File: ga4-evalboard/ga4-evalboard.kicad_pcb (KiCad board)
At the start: 2 copper layers, 21.6 x 21.5 mm, 8 parts, among them J1 power, J2 analog, J3 Conn_01x04_Male, J4 Conn_01x04_Male, U1 GA4, U4 SST25WF080B

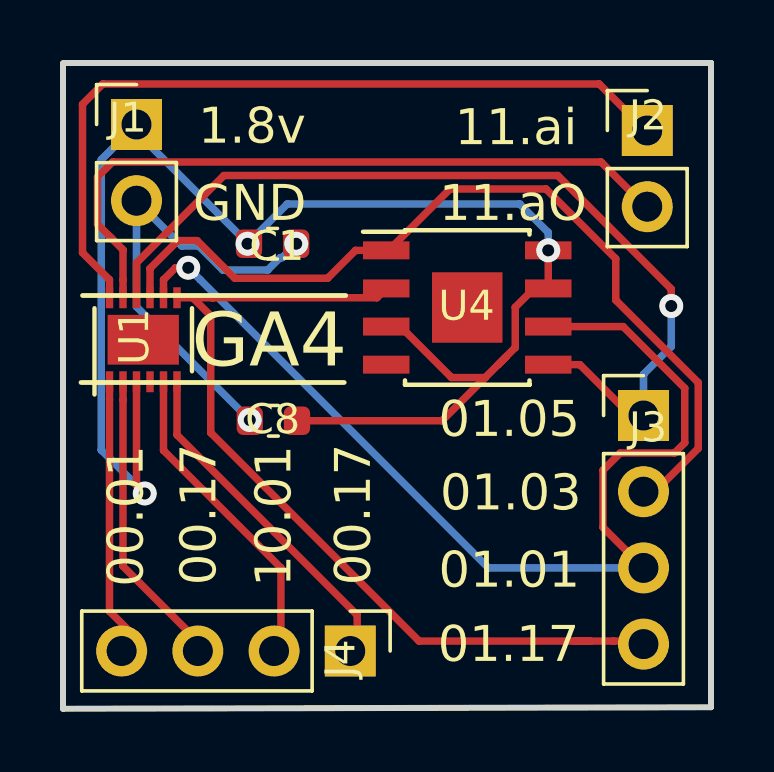
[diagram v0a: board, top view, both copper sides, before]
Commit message: ga4 evalboard layout changes
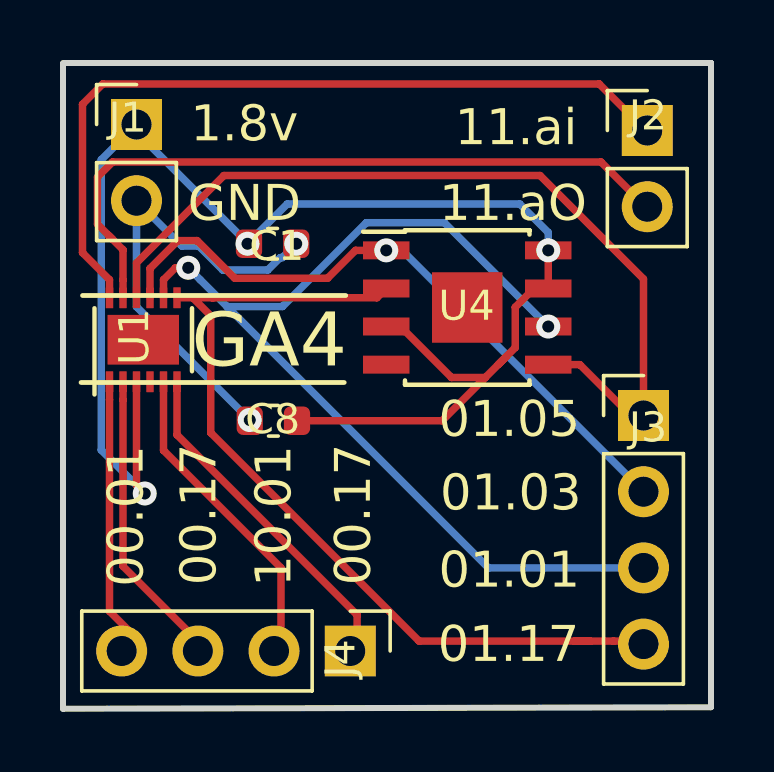
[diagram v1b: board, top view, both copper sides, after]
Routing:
- net 01.03: track 29.2 -> 22.0 mm, vias 0 -> 1
- net 01.05: track 30.2 -> 29.1 mm, vias 1 -> 0
- net 01.01: track 35.0 -> 34.2 mm, vias 1 -> 2
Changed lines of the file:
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@@
-(kicad_pcb (version 20171130) (host pcbnew 5.0.1-33cea8e~68~ubuntu14.04.1)
+(kicad_pcb (version 20171130) (host pcbnew 5.0.2-bee76a0~70~ubuntu14.04.1)
   (general
     (thickness 1.6)
     (drawings 19)
-    (tracks 122)
+    (tracks 111)
     (zones 0)
     (modules 8)
@@
     (effects (font (size 1.2 1.2) (thickness 0.25)))
   )
-  (gr_text GND (at 139.625 96.125) (layer F.SilkS)
-    (effects (font (size 1.2 1.2) (thickness 0.25)))
-  )
-  (gr_text 1.8v (at 139.7 93.55) (layer F.SilkS)
+  (gr_text GND (at 139.446 96.125) (layer F.SilkS)
+    (effects (font (size 1.2 1.2) (thickness 0.25)))
+  )
+  (gr_text 1.8v (at 139.446 93.472) (layer F.SilkS)
     (effects (font (size 1.2 1.2) (thickness 0.25)))
   )
@@
   )
   (via (at 139.625 103.35) (size 0.8) (drill 0.4) (layers F.Cu B.Cu) (net 1))
-  (via (at 139.55 97.475) (size 0.8) (drill 0.4) (layers F.Cu B.Cu) (net 2))
   (via (at 141.175 97.475) (size 0.8) (drill 0.4) (layers F.Cu B.Cu) (net 1))
   (segment (start 135.85 99.575) (end 139.625 103.35) (width 0.25) (layer B.Cu) (net 1))
@@
   (segment (start 140.225 98.35) (end 138.722682 98.35) (width 0.25) (layer B.Cu) (net 1))
   (segment (start 137.360159 97.550159) (end 135.85 96.04) (width 0.25) (layer B.Cu) (net 1))
-  (segment (start 135.4 98.675) (end 135.4 99.275) (width 0.25) (layer F.Cu) (net 4))
-  (segment (start 135.4 98.675) (end 135.4 97.675) (width 0.25) (layer F.Cu) (net 4))
-  (segment (start 135.05 97.325) (end 134.925 97.2) (width 0.25) (layer F.Cu) (net 4))
-  (segment (start 135.4 97.675) (end 135.05 97.325) (width 0.25) (layer F.Cu) (net 4))
-  (via (at 153.67516 99.54984) (size 0.8) (drill 0.4) (layers F.Cu B.Cu) (net 5))
+  (via (at 139.55 97.475) (size 0.8) (drill 0.4) (layers F.Cu B.Cu) (net 2))
   (segment (start 149.575 97.695) (end 149.575 97.695) (width 0.25) (layer F.Cu) (net 2))
   (via (at 136.125 105.8) (size 0.8) (drill 0.4) (layers F.Cu B.Cu) (net 2))
@@
   (segment (start 151.275 92.15) (end 134.725 92.15) (width 0.25) (layer F.Cu) (net 3))
   (segment (start 152.775 93.65) (end 151.275 92.15) (width 0.25) (layer F.Cu) (net 3))
+  (segment (start 135.4 98.675) (end 135.4 99.275) (width 0.25) (layer F.Cu) (net 4))
+  (segment (start 135.4 98.675) (end 135.4 97.675) (width 0.25) (layer F.Cu) (net 4))
+  (segment (start 135.05 97.325) (end 134.925 97.2) (width 0.25) (layer F.Cu) (net 4))
+  (segment (start 135.4 97.675) (end 135.05 97.325) (width 0.25) (layer F.Cu) (net 4))
   (segment (start 134.55 96.825) (end 135.05 97.325) (width 0.25) (layer F.Cu) (net 4))
   (segment (start 151.334978 94.749978) (end 135.050022 94.749978) (width 0.25) (layer F.Cu) (net 4))
@@
   (segment (start 150.63 101.505) (end 152.325 103.2) (width 0.25) (layer F.Cu) (net 5))
   (segment (start 149.575 101.505) (end 150.63 101.505) (width 0.25) (layer F.Cu) (net 5))
-  (segment (start 153.67516 100.89984) (end 153.67516 99.54984) (width 0.25) (layer B.Cu) (net 5))
-  (segment (start 152.75 101.825) (end 153.67516 100.89984) (width 0.25) (layer B.Cu) (net 5))
-  (segment (start 152.75 103.2) (end 152.75 101.825) (width 0.25) (layer B.Cu) (net 5))
-  (segment (start 149.890994 95.199989) (end 153.67516 98.984155) (width 0.25) (layer F.Cu) (net 5))
+  (segment (start 152.75 98.648) (end 152.75 103.2) (width 0.25) (layer F.Cu) (net 5))
+  (segment (start 149.301989 95.199989) (end 152.75 98.648) (width 0.25) (layer F.Cu) (net 5))
+  (segment (start 138.7636 95.199989) (end 149.301989 95.199989) (width 0.25) (layer F.Cu) (net 5))
+  (segment (start 135.85 98.113589) (end 138.7636 95.199989) (width 0.25) (layer F.Cu) (net 5))
   (segment (start 135.85 99.275) (end 135.85 98.113589) (width 0.25) (layer F.Cu) (net 5))
-  (segment (start 138.7636 95.199989) (end 149.890994 95.199989) (width 0.25) (layer F.Cu) (net 5))
-  (segment (start 135.85 98.113589) (end 138.7636 95.199989) (width 0.25) (layer F.Cu) (net 5))
-  (segment (start 153.67516 98.984155) (end 153.67516 99.54984) (width 0.25) (layer F.Cu) (net 5))
   (segment (start 136.3 98.3) (end 136.3 99.275) (width 0.25) (layer F.Cu) (net 6))
   (segment (start 137.870057 97.370057) (end 137.229943 97.370057) (width 0.25) (layer F.Cu) (net 6))
@@
   (segment (start 143.15 97.695) (end 142.22 98.625) (width 0.25) (layer F.Cu) (net 6))
   (segment (start 144.175 97.695) (end 143.15 97.695) (width 0.25) (layer F.Cu) (net 6))
-  (segment (start 153.231413 105.64) (end 152.95 105.64) (width 0.25) (layer F.Cu) (net 6))
-  (segment (start 154.57499 104.296423) (end 153.231413 105.64) (width 0.25) (layer F.Cu) (net 6))
-  (segment (start 154.57499 102.103577) (end 154.57499 104.296423) (width 0.25) (layer F.Cu) (net 6))
-  (segment (start 151.825 99.353587) (end 154.57499 102.103577) (width 0.25) (layer F.Cu) (net 6))
-  (segment (start 151.825 97.975) (end 151.825 99.353587) (width 0.25) (layer F.Cu) (net 6))
-  (segment (start 149.5 95.65) (end 151.825 97.975) (width 0.25) (layer F.Cu) (net 6))
-  (segment (start 146.3 95.65) (end 149.5 95.65) (width 0.25) (layer F.Cu) (net 6))
-  (segment (start 144.255 97.695) (end 146.3 95.65) (width 0.25) (layer F.Cu) (net 6))
-  (segment (start 144.175 97.695) (end 144.255 97.695) (width 0.25) (layer F.Cu) (net 6))
+  (via (at 144.175 97.695) (size 0.8) (drill 0.4) (layers F.Cu B.Cu) (net 6))
+  (segment (start 144.705 97.695) (end 144.175 97.695) (width 0.25) (layer B.Cu) (net 6))
+  (segment (start 152.75 105.74) (end 144.705 97.695) (width 0.25) (layer B.Cu) (net 6))
   (segment (start 136.75 98.675) (end 137.14984 98.27516) (width 0.25) (layer F.Cu) (net 7))
   (segment (start 136.75 99.275) (end 136.75 98.675) (width 0.25) (layer F.Cu) (net 7))
-  (segment (start 147.57968 108.28) (end 137.974839 98.675159) (width 0.25) (layer B.Cu) (net 7))
   (segment (start 137.14984 98.27516) (end 137.57484 98.27516) (width 0.25) (layer F.Cu) (net 7))
   (via (at 137.57484 98.27516) (size 0.8) (drill 0.4) (layers F.Cu B.Cu) (net 7))
   (segment (start 137.974839 98.675159) (end 137.57484 98.27516) (width 0.25) (layer B.Cu) (net 7))
   (segment (start 152.75 108.28) (end 147.57968 108.28) (width 0.25) (layer B.Cu) (net 7))
-  (segment (start 151.4 106.93) (end 152.75 108.28) (width 0.25) (layer F.Cu) (net 7))
-  (segment (start 151.4 105.025) (end 151.4 106.93) (width 0.25) (layer F.Cu) (net 7))
-  (segment (start 151.975 104.45) (end 151.4 105.025) (width 0.25) (layer F.Cu) (net 7))
-  (segment (start 153.785002 104.45) (end 151.975 104.45) (width 0.25) (layer F.Cu) (net 7))
-  (segment (start 154.124979 104.110023) (end 153.785002 104.45) (width 0.25) (layer F.Cu) (net 7))
-  (segment (start 154.124979 102.289977) (end 154.124979 104.110023) (width 0.25) (layer F.Cu) (net 7))
-  (segment (start 152.070002 100.235) (end 154.124979 102.289977) (width 0.25) (layer F.Cu) (net 7))
-  (segment (start 149.575 100.235) (end 152.070002 100.235) (width 0.25) (layer F.Cu) (net 7))
+  (segment (start 138.86768 99.568) (end 140.716 99.568) (width 0.25) (layer B.Cu) (net 7))
+  (segment (start 147.57968 108.28) (end 138.86768 99.568) (width 0.25) (layer B.Cu) (net 7))
+  (segment (start 138.86768 99.568) (end 137.974839 98.675159) (width 0.25) (layer B.Cu) (net 7))
+  (segment (start 140.716 99.568) (end 143.51 96.774) (width 0.25) (layer B.Cu) (net 7))
+  (segment (start 146.114 96.774) (end 149.575 100.235) (width 0.25) (layer B.Cu) (net 7))
+  (segment (start 143.51 96.774) (end 146.114 96.774) (width 0.25) (layer B.Cu) (net 7))
+  (segment (start 149.575 100.235) (end 149.575 100.235) (width 0.25) (layer B.Cu) (net 7))
+  (via (at 149.575 100.235) (size 0.8) (drill 0.4) (layers F.Cu B.Cu) (net 7))
   (segment (start 151.747919 110.72) (end 152.95 110.72) (width 0.25) (layer F.Cu) (net 8))
   (segment (start 143.865 99.275) (end 144.175 98.965) (width 0.25) (layer F.Cu) (net 8))
